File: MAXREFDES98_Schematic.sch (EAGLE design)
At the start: 34 parts, among them U1 MB110S-TP, U2 MB110S-TP, U3 MAX5969AETB+

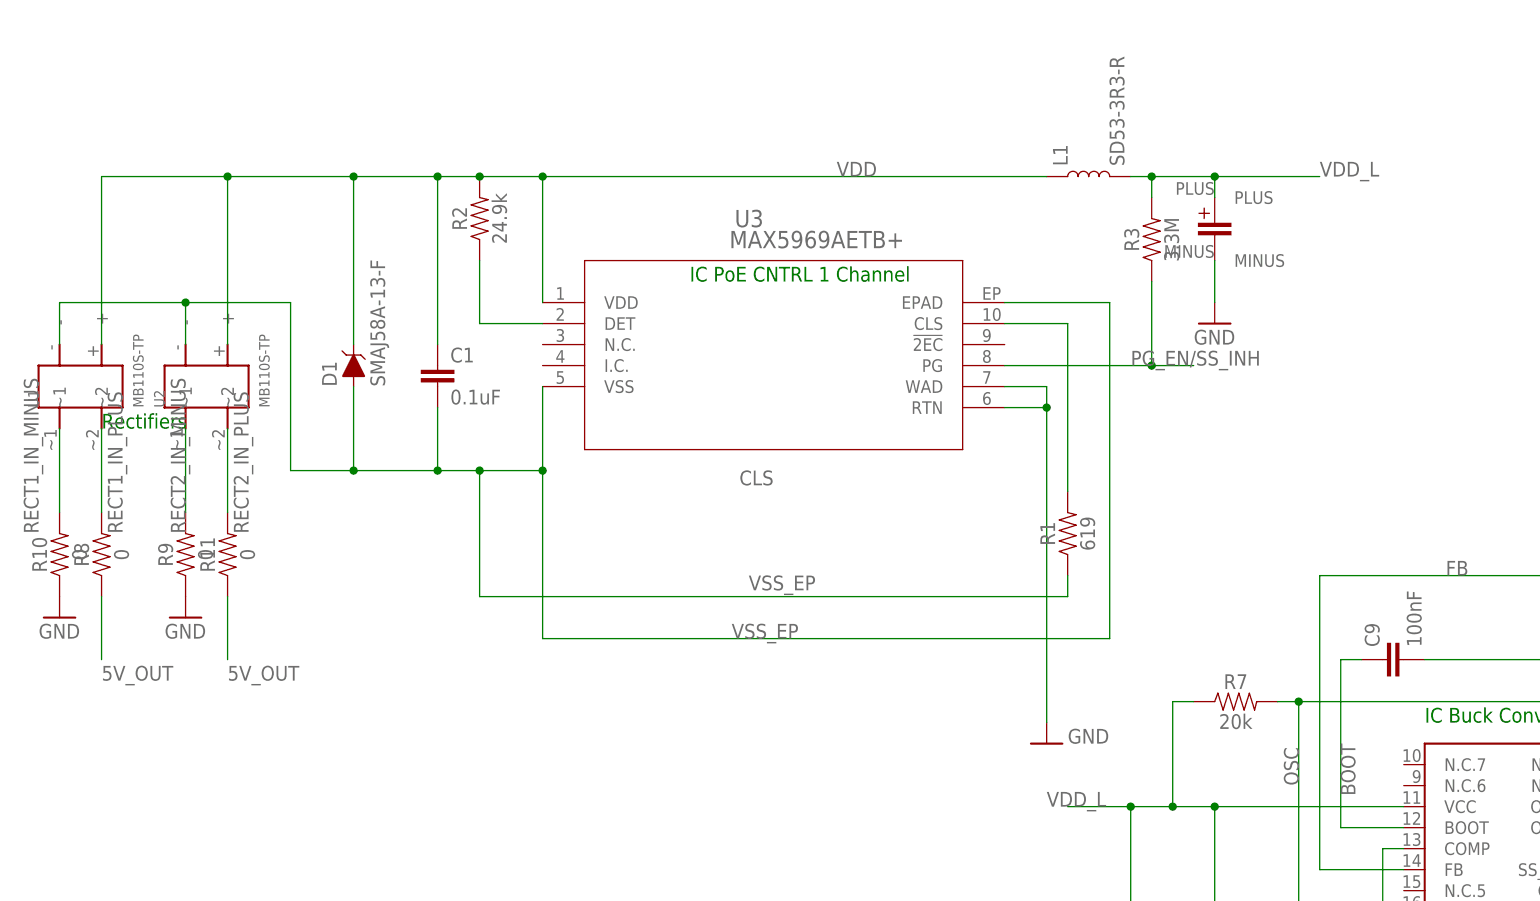
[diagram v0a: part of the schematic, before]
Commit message: Deleted PoE and added Transformer
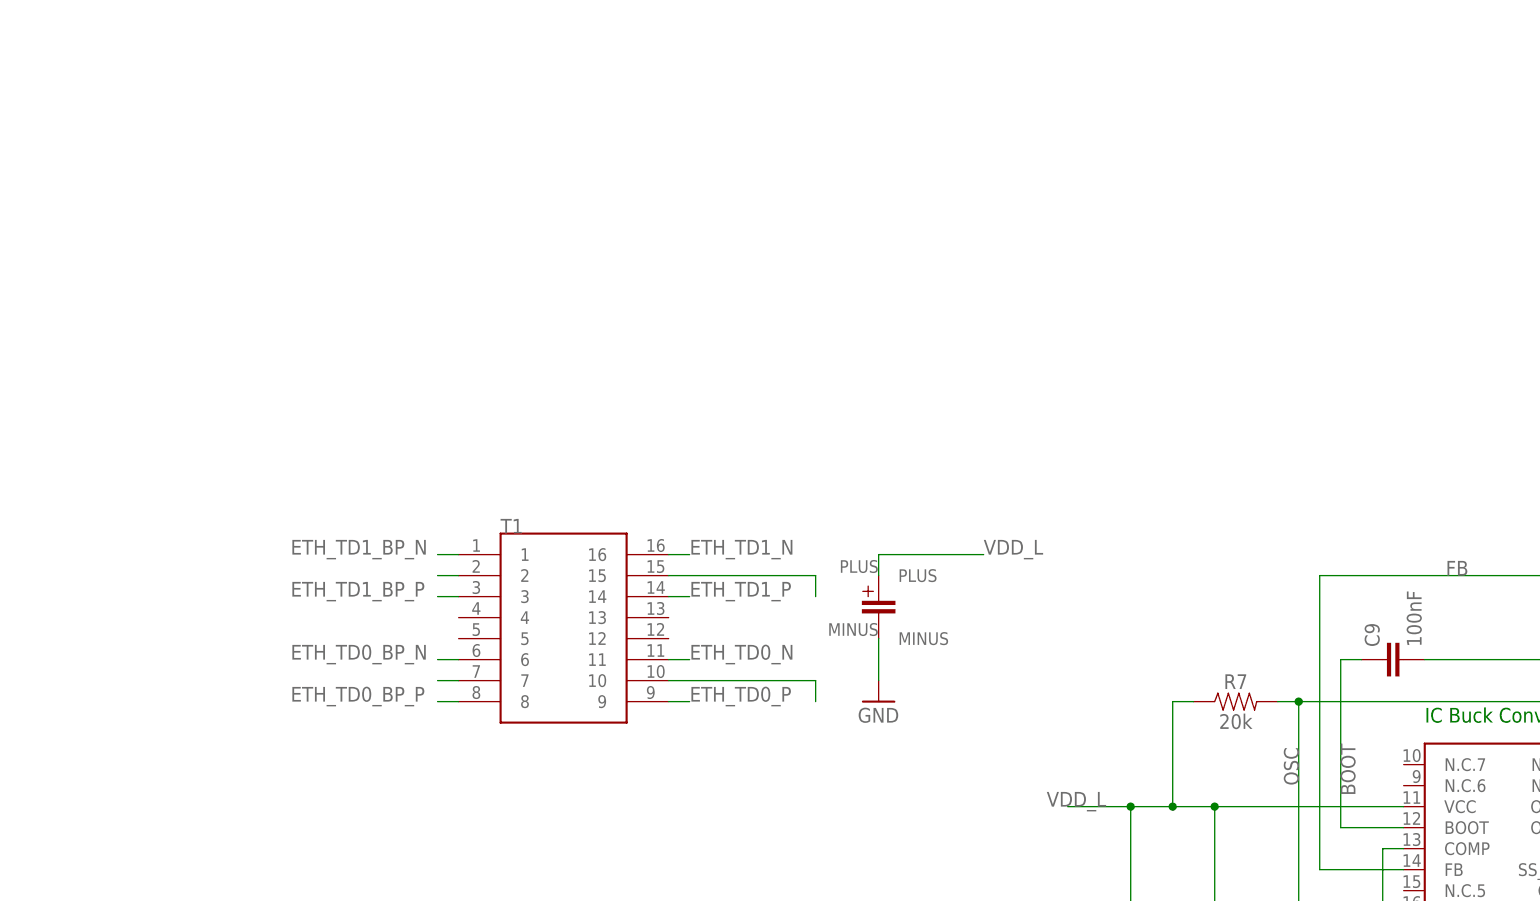
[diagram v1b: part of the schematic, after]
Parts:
- removed C1: 0.1uF, SparkFun-Capacitors:0.1UF-0603-25V-5%
- removed D1: SMAJ58A-13-F, SMAJ58A-13-F:SMAJ58A-13-F
- removed L1: SD53-3R3-R, SD53-3R3-R:SD53-3R3-R
- removed R1: 619, SparkFun-Resistors:0.05OHM-0603-1/5W-1%
- removed R10, R11, R8, R9: 0, SparkFun-Resistors:0OHM-0603-1/10W-5%
- removed R2: 24.9k, SparkFun-Resistors:0.05OHM-0603-1/5W-1%
- removed R3: 3.3M, SparkFun-Resistors:0.05OHM-0603-1/5W-1%
- removed U1, U2: MB110S-TP, MB110S-TP:MB110S-TP
- removed U3: MAX5969AETB+, MAX5969AETB+_Library:MAX5969AETB+
- added T1: TG110-S055N2RL, CameraBoard_Library:TG110-S055N2RL
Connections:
- removed net CLS: R1.2, U3.CLS
- removed net DET: R2.1, U3.DET
- removed net VDD: C1.1, D1.1, L1.1, R2.2, U1.+, U2.+, U3.VDD
- removed net VSS_EP: C1.2, D1.2, R1.1, U1.-, U2.-, U3.EPAD, U3.VSS
- new net ETH_TD0_BP_N: T1.6
- new net ETH_TD0_BP_P: T1.8
- new net ETH_TD0_N: T1.11
- new net ETH_TD0_P: T1.9
- new net ETH_TD1_BP_N: T1.1
- new net ETH_TD1_BP_P: T1.3
- new net ETH_TD1_N: T1.16
- new net ETH_TD1_P: T1.14
- new net N$11: T1.2
- new net N$14: T1.7
- new net N$4: T1.10
- new net N$5: T1.15
- net 5V_OUT: no longer R11.1, R8.1
- net GND: no longer R10.1, R9.1, U3.RTN, U3.WAD
- net PG_EN/SS_INH: no longer R3.1, U3.PG
- net RECT1_IN_MINUS: no longer R10.2, U1.~1
- net RECT1_IN_PLUS: no longer R8.2, U1.~2
- net RECT2_IN_MINUS: no longer R9.2, U2.~1
- net RECT2_IN_PLUS: no longer R11.2, U2.~2
- net VDD_L: no longer L1.2, R3.2
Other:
- note removed: "IC PoE CNTRL 1 Channel"
- note removed: "Rectifiers"

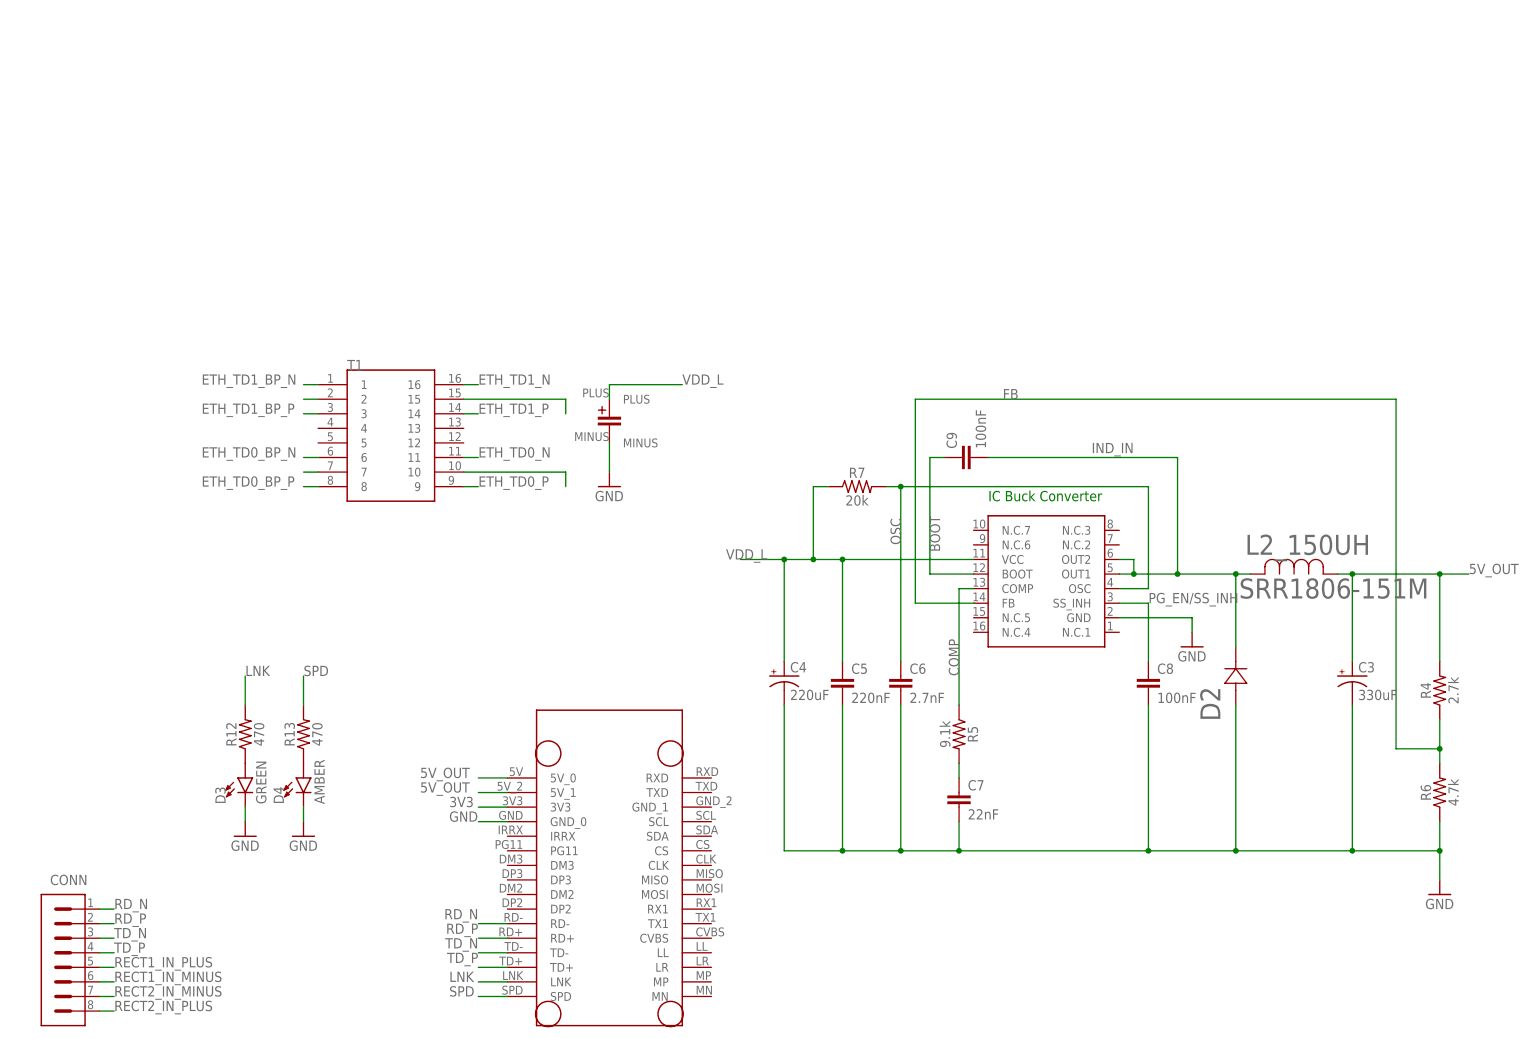
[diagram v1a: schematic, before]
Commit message: Updated board with transformer circuit and new connector signals
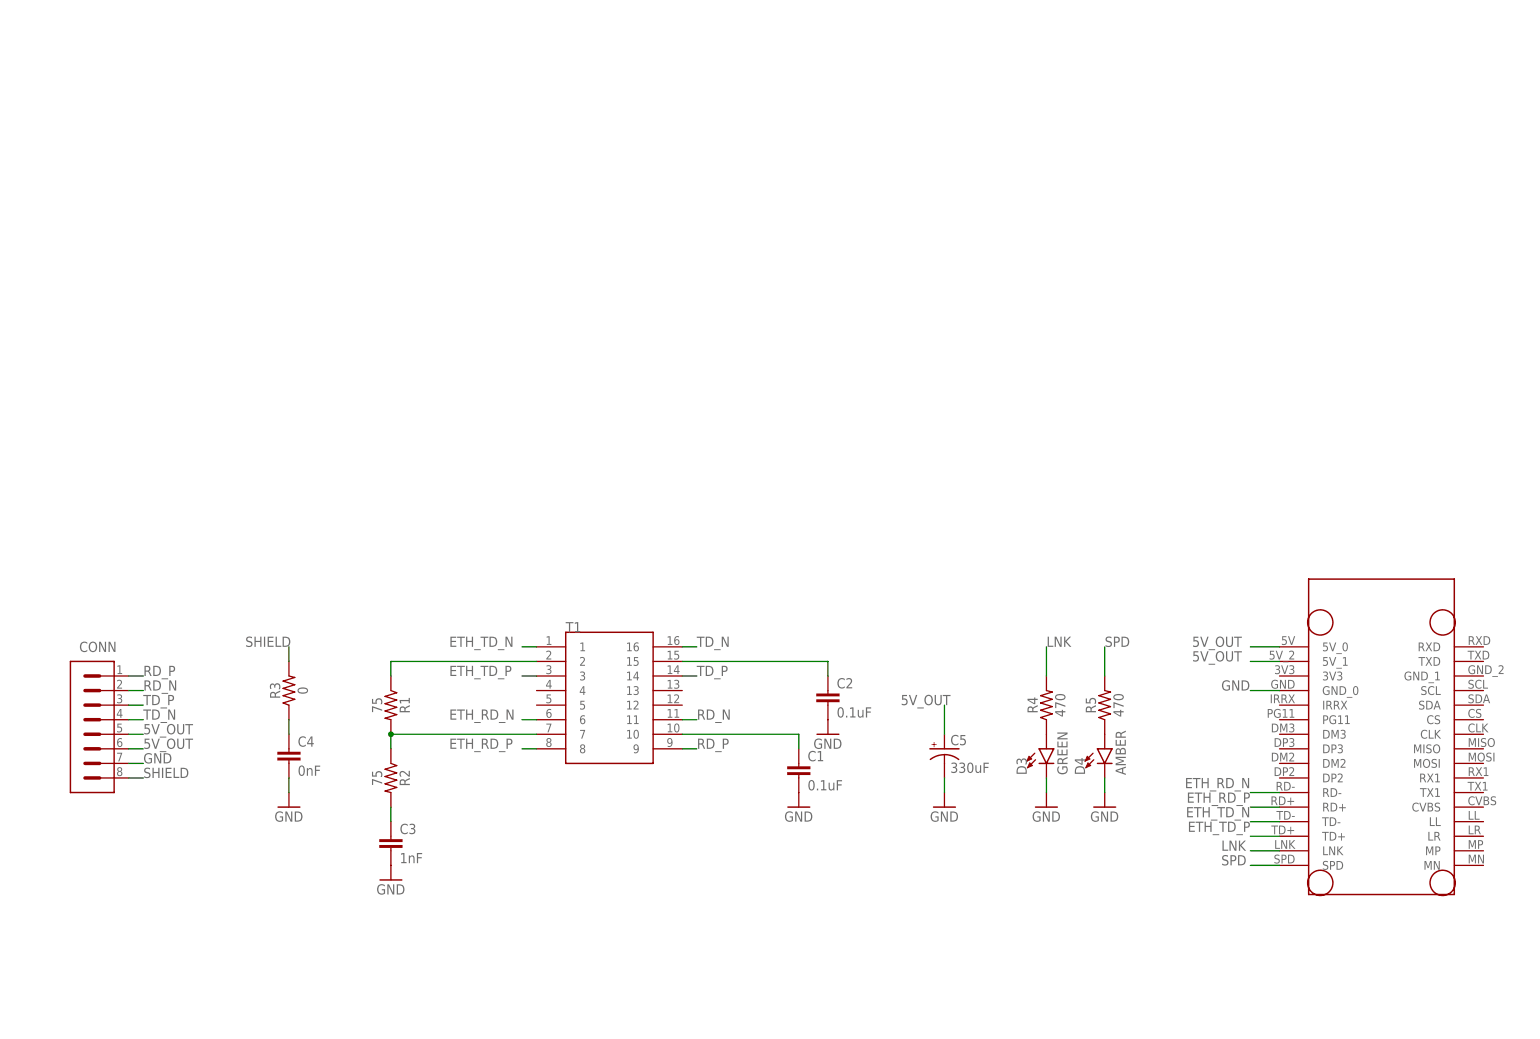
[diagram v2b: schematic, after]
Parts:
- removed C6: 2.7nF, SparkFun-Capacitors:4.7UF0603
- removed C7: 22nF, SparkFun-Capacitors:4.7UF0603
- removed C8, C9: 100nF, SparkFun-Capacitors:4.7UF0603
- removed D2: STPS3L60USMB_STM-M, Camera_Board_Parts_09_30_2020:STPS3L60USMB_STM-M
- removed L2_150UH: SRR1806-151M, CameraBoard_Library:SRR1806-151M
- removed R12, R13: 470, SparkFun-Resistors:0OHM-0603-1/10W-5%
- removed R6: 4.7k, SparkFun-Resistors:470OHM-0603-1/10W-1%
- removed R7: 20k, SparkFun-Resistors:22KOHM-0603-1/10W-1%
- removed U$1: L4978D013TR, Camera_Board_Parts_09_30_2020:L4978D013TR
- added C1: 0.1uF, SparkFun-Capacitors:0.1UF-0603-25V-(+80/-20%)
- added R1, R2: 75, SparkFun-Resistors:75KOHM-0603-1/10W-1%
- added R3: 0, SparkFun-Resistors:0OHM-0603-1/10W-5%
- C2: value EEE-1JA220UP -> 0.1uF; device EEE-1JA220UP:EEE-1JA220UP -> SparkFun-Capacitors:0.1UF-0603-25V-(+80/-20%)
- C3: value 337AXZ025M -> 1nF; device CameraBoard_Library:337AXZ025M -> SparkFun-Capacitors:1.0NF/1000PF-0603-50V-10%
- C4: value EXV227M016A9HAA -> 0nF; device CameraBoard_Library:EXV227M016A9HAA -> SparkFun-Capacitors:3.3NF-0603-100V-10%
- C5: value 220nF -> 337AXZ025M; device SparkFun-Capacitors:4.7UF0603 -> CameraBoard_Library:337AXZ025M
- R4: value 2.7k -> 470; device SparkFun-Resistors:20OHM-0603-1/10W-1% -> SparkFun-Resistors:0OHM-0603-1/10W-5%
- R5: value 9.1k -> 470; device SparkFun-Resistors:470OHM-0603-1/10W-1% -> SparkFun-Resistors:0OHM-0603-1/10W-5%
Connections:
- removed net 3V3: U$2.3V3
- removed net BOOT: C9.1, U$1.BOOT
- removed net COMP: R5.1, U$1.COMP
- removed net ETH_TD0_BP_N: T1.6
- removed net ETH_TD0_BP_P: T1.8
- removed net ETH_TD0_N: T1.11
- removed net ETH_TD0_P: T1.9
- removed net ETH_TD1_BP_N: T1.1
- removed net ETH_TD1_BP_P: T1.3
- removed net ETH_TD1_N: T1.16
- removed net ETH_TD1_P: T1.14
- removed net FB: R4.1, R6.2, U$1.FB
- removed net IND_IN: C9.2, D2.1, L2_150UH.2, U$1.OUT1, U$1.OUT2
- removed net N$5: T1.15
- removed net N$6: C7.1, R5.2
- removed net OSC: C6.1, R7.2, U$1.OSC
- removed net PG_EN/SS_INH: C8.1, U$1.SS_INH
- removed net RECT1_IN_MINUS: CONN.6
- removed net RECT1_IN_PLUS: CONN.5
- removed net RECT2_IN_MINUS: CONN.7
- removed net RECT2_IN_PLUS: CONN.8
- removed net VDD_L: C2.PLUS, C4.+, C5.1, R7.1, U$1.VCC
- new net ETH_RD_N: T1.6, U$2.RD-
- new net ETH_RD_P: T1.8, U$2.RD+
- new net ETH_TD0_GND: C1.1, T1.10
- new net ETH_TD1_GND: C2.1, T1.15
- new net ETH_TD_N: T1.1, U$2.TD-
- new net ETH_TD_P: T1.3, U$2.TD+
- new net N$3: C3.1, R2.2
- new net SHIELD: CONN.8, R3.2
- net 5V_OUT: now also C5.+, CONN.5, CONN.6; no longer C3.+, L2_150UH.1, R4.2
- net GND: now also C1.2, C2.2, C3.2, C4.2, C5.-, CONN.7; no longer C2.MINUS, C3.-, C4.-, C5.2, C6.2, C7.2, C8.2, D2.2, R6.1, U$1.GND
- net LNK: now also R4.2; no longer R12.2
- net N$1: now also R4.1; no longer R12.1
- net N$11: now also R1.1
- net N$14: now also R1.2, R2.1
- net N$2: now also R5.1; no longer R13.1
- net N$4: now also C4.1, R3.1; no longer T1.10
- net RD_N: now also CONN.2, T1.11; no longer CONN.1, U$2.RD-
- net RD_P: now also CONN.1, T1.9; no longer CONN.2, U$2.RD+
- net SPD: now also R5.2; no longer R13.2
- net TD_N: now also CONN.4, T1.16; no longer CONN.3, U$2.TD-
- net TD_P: now also CONN.3, T1.14; no longer CONN.4, U$2.TD+
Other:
- note removed: "IC Buck Converter"
- moved on the sheet: CONN, D3, D4, R4, R5, T1
